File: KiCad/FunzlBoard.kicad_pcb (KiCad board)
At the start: 2 copper layers, 174 x 149 mm, 63 parts, among them SW1 SW_MEC_5E, SW2 SW_MEC_5E, SW3 SW_MEC_5E, SW4 SW_MEC_5E, U1 ESP32-C3_SUPERMINI_SMD, U2 ADS7828, U3 MCP23017_SO

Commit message: Add DIP Switch to PCB
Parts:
- added SW5: SW_MEC_5E, Button_Switch_THT:SW_PUSH_6mm_H13mm, F.Cu at (158.0, 90.0)
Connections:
- U3 pad 5: unconnected-(U3-GPB4-Pad5) -> Net-(U3-GPB4)

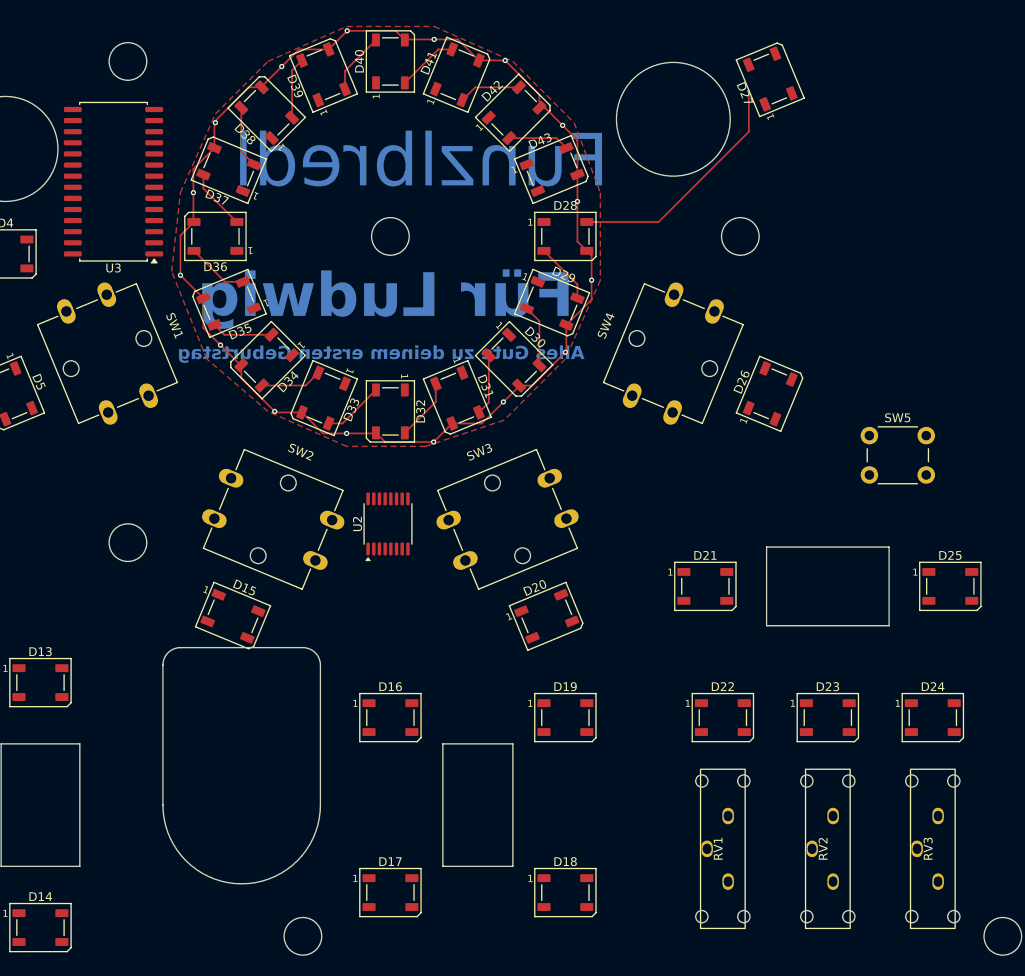
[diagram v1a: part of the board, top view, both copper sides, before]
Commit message: Move a screw
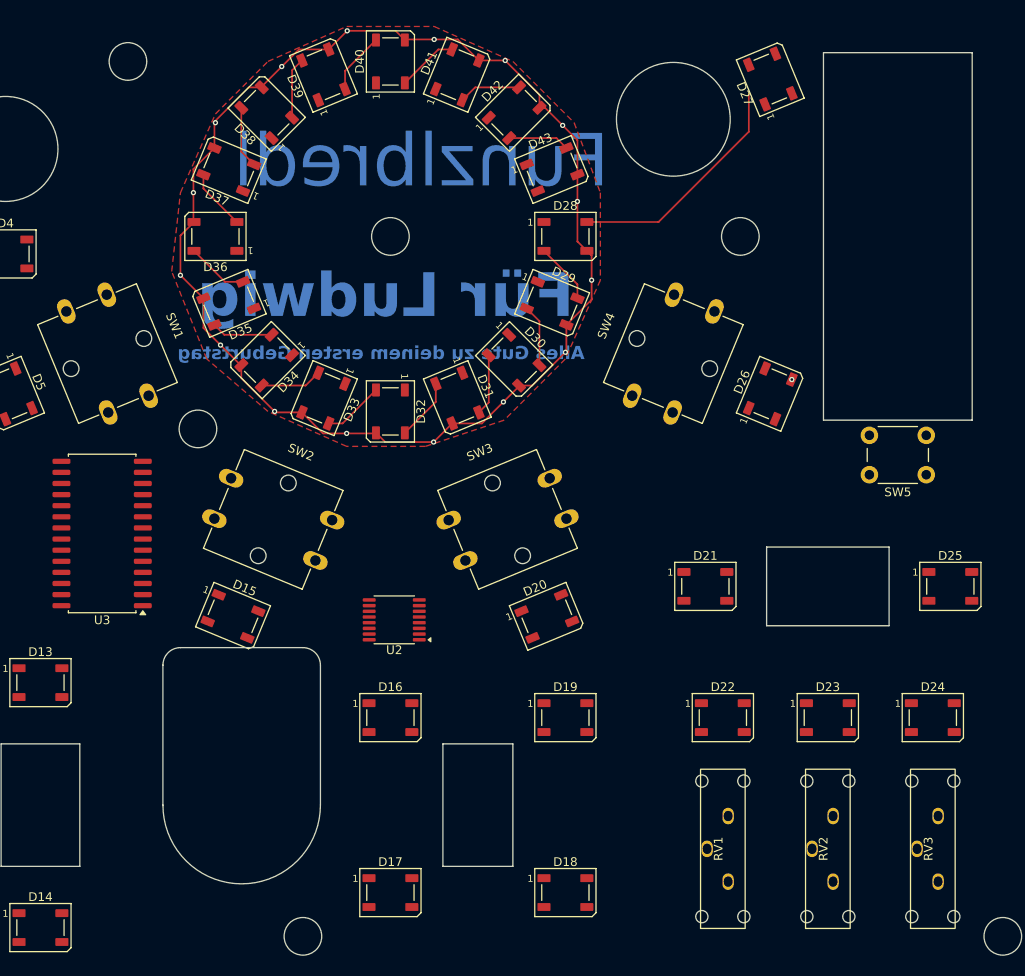
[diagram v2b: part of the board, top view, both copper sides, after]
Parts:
- moved U3 40.2 mm to (67.0, 99.0)
- moved H6 15.3 mm to (78.0, 87.0)
- moved U2 11.0 mm to (100.4, 108.8), turned to 180 degrees
- turned SW5 to 180 degrees
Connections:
- SW1 pad 1: unconnected-(SW1-Pad1) -> Net-(U3-GPB0)
- SW1 pad 4: unconnected-(SW1-A-Pad4) -> GND
- SW2 pad 1: unconnected-(SW2-Pad1) -> Net-(U3-GPB1)
- SW2 pad 4: unconnected-(SW2-A-Pad4) -> GND
- SW3 pad 1: unconnected-(SW3-Pad1) -> Net-(U3-GPB2)
- SW3 pad 4: unconnected-(SW3-A-Pad4) -> GND
- SW4 pad 1: unconnected-(SW4-Pad1) -> Net-(U3-GPB3)
- SW4 pad 4: unconnected-(SW4-A-Pad4) -> GND
- SW5 pad 1: unconnected-(SW5-Pad1)_1 -> Net-(U3-GPB4)
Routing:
- net GND: vias 16 -> 17
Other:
- outline, holes or cut-outs redrawn

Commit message: Add Trimmer
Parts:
- added RV5: R_Potentiometer, Lib:TrimmerH, B.Cu at (175.3, 95.0)
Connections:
- RV1 pad 1: +3V3 -> REF
- RV2 pad 1: +3V3 -> REF
- RV3 pad 1: +3V3 -> REF
- U2 pad 10: unconnected-(U2-REF-Pad10) -> REF
- U2 pad 7: +3V3 -> unconnected-(U2-CH6-Pad7)
- U2 pad 8: GND -> unconnected-(U2-CH7-Pad8)
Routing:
- net Net-(D27-DOUT): track 27.2 -> 28.0 mm
